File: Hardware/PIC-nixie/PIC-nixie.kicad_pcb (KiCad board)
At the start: 2 copper layers, 100 x 35 mm, 56 parts, among them J1 DX07S024WJ3R400, J2 Conn_01x20_Female, M1 TP5335, M2 TP5335, M3 TP5335, M4 TP5335, Q1 PMBTA42,185, Q2 PMBTA42,185, Q3 PMBTA42,185, Q4 PMBTA42,185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

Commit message: logic PCB tweaks, resize
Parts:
- removed the REF** at (205.0, 75.0)
- removed the REF** at (124.0, 90.0)
- added REF**: MountingHole_2.2mm_M2, MountingHole:MountingHole_2.2mm_M2, F.Cu at (125.0, 88.0)
- added REF**: MountingHole_2.2mm_M2, MountingHole:MountingHole_2.2mm_M2, F.Cu at (195.0, 88.0)
- moved SW3 37.7 mm to (136.2, 90.0)
- moved RA7 26.2 mm to (153.5, 97.4)
- moved J1 25.9 mm to (178.8, 88.5), turned to 0 degrees
- moved RA3 23.6 mm to (145.1, 97.5), turned to 270 degrees
- moved J2 22.4 mm to (161.4, 120.5)
- moved U2 21.5 mm to (121.8, 113.8)
- moved XTAL1 21.5 mm to (121.6, 109.1)
- moved C1 21.5 mm to (112.6, 96.2)
- moved C10 21.5 mm to (120.2, 104.1)
- moved C11 21.5 mm to (191.6, 118.0)
- moved C12 21.5 mm to (183.5, 99.4)
- moved C2 21.5 mm to (111.6, 117.5)
- moved C3 21.5 mm to (106.0, 106.8)
- moved C4 21.5 mm to (129.6, 106.3)
- moved C5 21.5 mm to (126.6, 108.9)
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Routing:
- net GND: track 257.5 -> 161.6 mm, vias 64 -> 65
- net Net-(RA1-Pad7): track 39.9 -> 73.4 mm
- net Net-(RA1-Pad5): track 75.8 -> 54.5 mm
- net Net-(RA1-Pad6): track 56.9 -> 68.2 mm, vias 1 -> 0
- net Net-(RA3-Pad2): track 3.22 -> 10.7 mm
- net /MIN1: track 27.8 -> 31.0 mm
- net /colon1: track 29.7 -> 26.6 mm, vias 2 -> 1
- net /HR1: track 25.9 -> 28.7 mm
- net Net-(M4-Pad1): track 11.6 -> 8.86 mm
- net Net-(M1-Pad1): track 15.6 -> 17.7 mm
- net Net-(M2-Pad1): track 13.1 -> 15.1 mm
- net VCC: track 210.8 -> 209.0 mm, vias 5 -> 6
- net Net-(M3-Pad1): track 10.6 -> 12.3 mm
- net /colon2: track 28.4 -> 30.0 mm
- net Net-(RA3-Pad3): track 15.5 -> 17.0 mm
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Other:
- board size 100 x 35 mm -> 100 x 40 mm

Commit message: PCB as submitted to fab
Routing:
- net GND: track 161.6 -> 157.7 mm
- net /MIN1: track 31.0 -> 29.9 mm
- net /HR1: track 28.7 -> 27.9 mm

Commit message: fix switch pin assignment, reduce hole size on nixie sockets
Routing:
- net Net-(RA1-Pad6): track 68.2 -> 50.9 mm, vias 0 -> 1
- net Net-(RA1-Pad5): track 54.5 -> 43.7 mm
- net Net-(RA1-Pad7): track 73.4 -> 66.1 mm, vias 1 -> 0

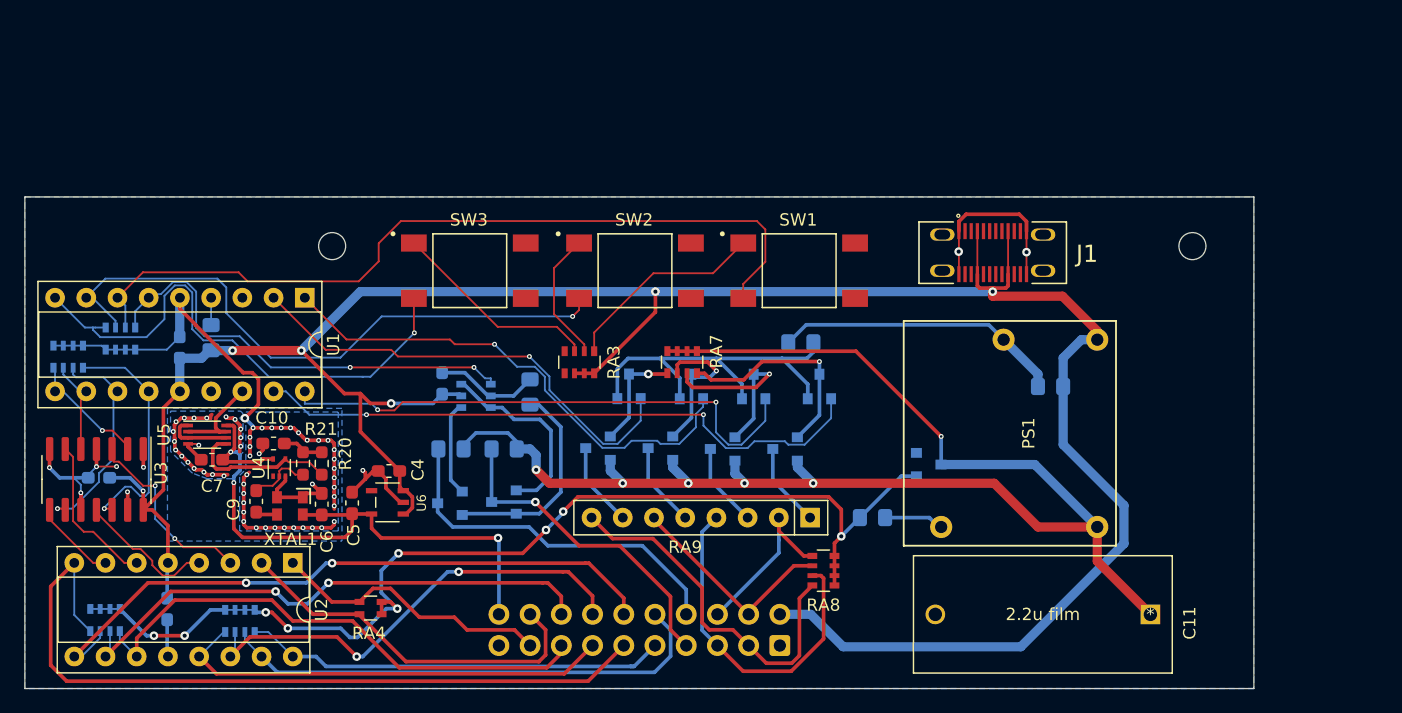
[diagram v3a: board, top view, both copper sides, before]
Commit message: add battery backup for power failures
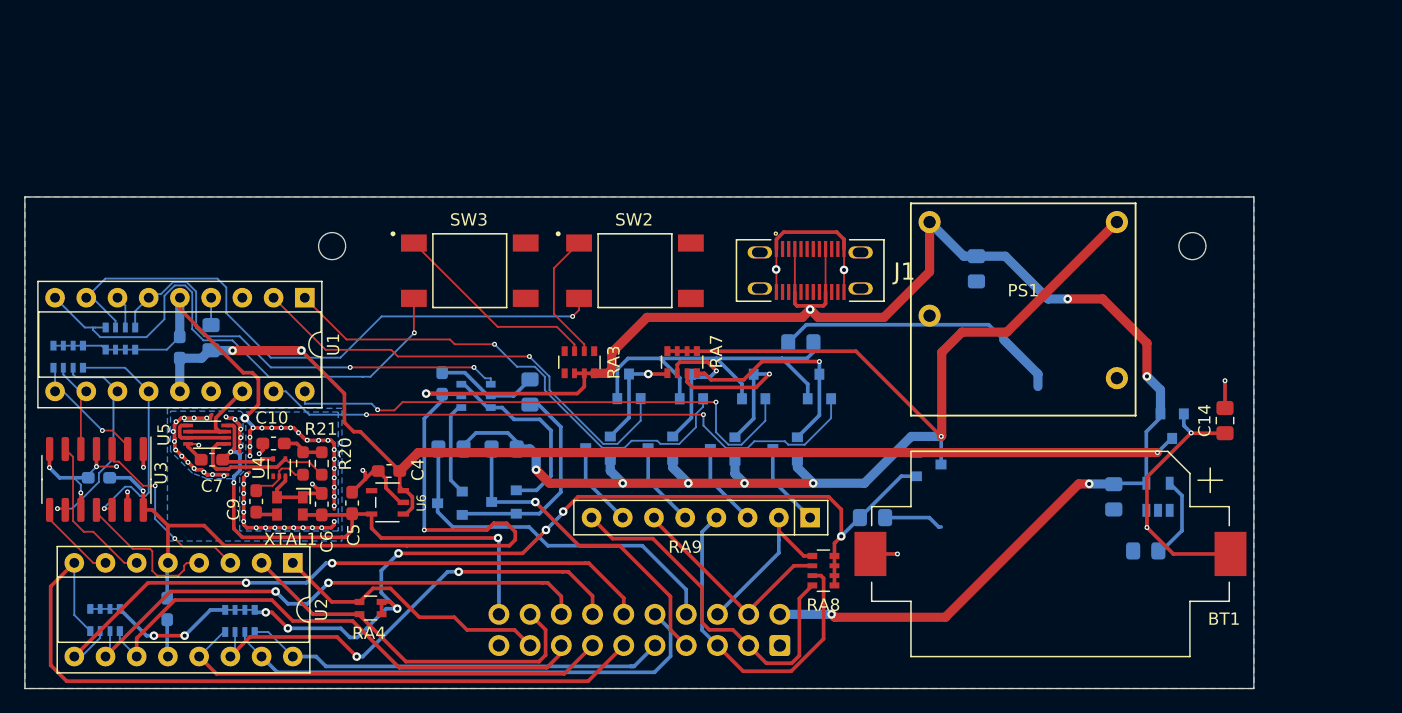
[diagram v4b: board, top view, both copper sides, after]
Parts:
- removed C11: 2.2u film, external:ECQ-E2275JB
- removed SW1: SW_SPST, external:SW_TL3301SPF260QG
- added BT1: rjd2032C1, Battery:BatteryHolder_Keystone_1060_1x2032, F.Cu at (183.4, 113.0)
- added C13: 4.7u, Capacitor_SMD:C_0805_2012Metric_Pad1.15x1.40mm_HandSolder, B.Cu at (188.6, 108.4)
- added C14: 4.7u, Capacitor_SMD:C_0805_2012Metric_Pad1.15x1.40mm_HandSolder, F.Cu at (197.7, 102.2)
- added D2: BAT54C, Package_TO_SOT_SMD:SOT-23, B.Cu at (193.3, 102.7)
- added R2: 28k, Resistor_SMD:R_0805_2012Metric_Pad1.15x1.40mm_HandSolder, B.Cu at (191.2, 112.8)
- added U8: MCP73832-2-OT, Package_TO_SOT_SMD:SOT-23-5, B.Cu at (192.2, 108.4)
- moved J1 14.9 mm to (163.9, 90.0)
- moved PS1 12.1 mm to (181.2, 91.1), turned to 0 degrees
- moved C12 11.3 mm to (177.4, 89.8), turned to 270 degrees
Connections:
- C1 pad 1: VCC -> Net-(C1-Pad1)
- C4 pad 1: VCC -> Net-(C1-Pad1)
- R1 pad 1: VCC -> Net-(C1-Pad1)
- U1 pad 14: VCC -> Net-(C1-Pad1)
- U6 pad 1: VCC -> Net-(C1-Pad1)
- U6 pad 3: VCC -> Net-(C1-Pad1)
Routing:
- net Net-(C1-Pad1): track 0.00 -> 94.8 mm, vias 0 -> 3
- net Net-(RA1-Pad7): track 66.1 -> 2.69 mm
- net Net-(BT1-Pad1): track 0.00 -> 22.9 mm, vias 0 -> 2
- net Net-(RA3-Pad1): track 16.7 -> 0.00 mm
- net Vdrive: track 117.3 -> 106.5 mm
- net VCC: track 209.0 -> 198.3 mm, vias 6 -> 8
- net Net-(R2-Pad1): track 0.00 -> 6.87 mm
- net GND: track 157.7 -> 162.1 mm, vias 65 -> 67
- net Net-(U2-Pad4): track 11.3 -> 12.3 mm

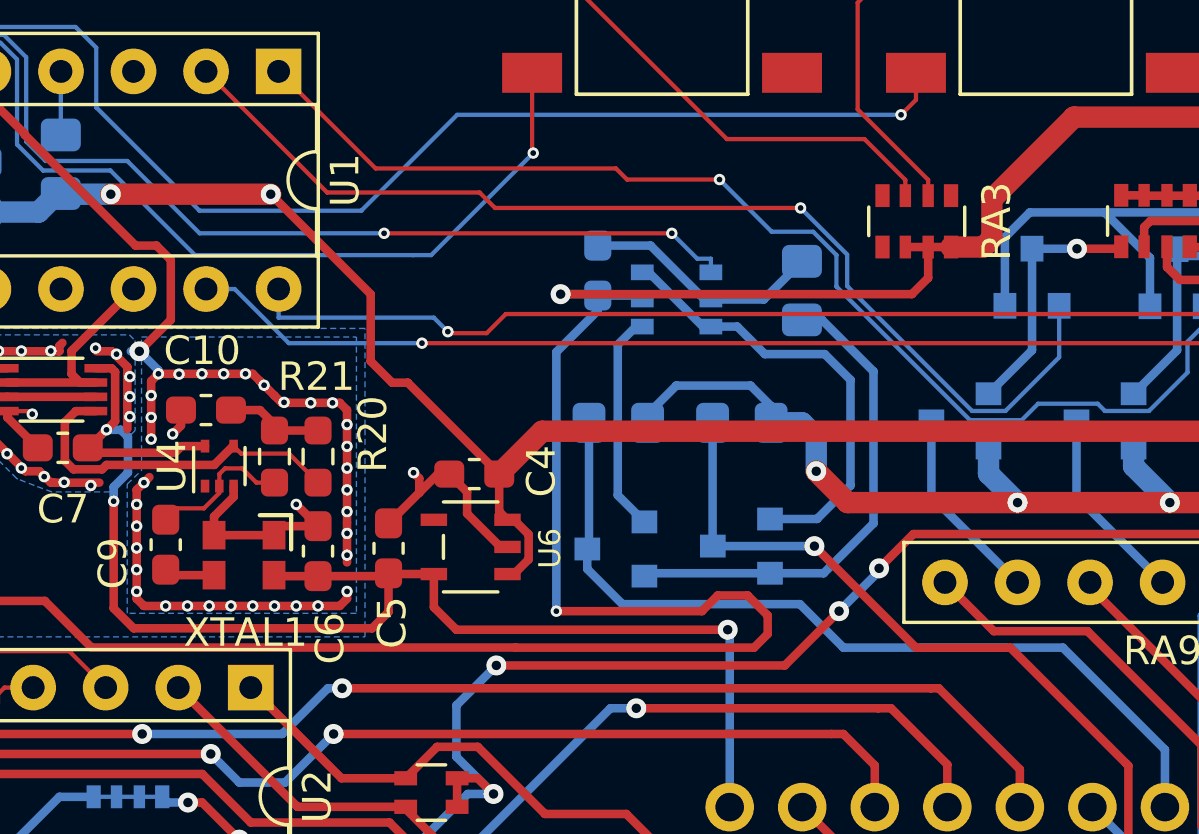
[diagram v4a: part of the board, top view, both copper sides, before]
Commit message: update 3D view, add figures
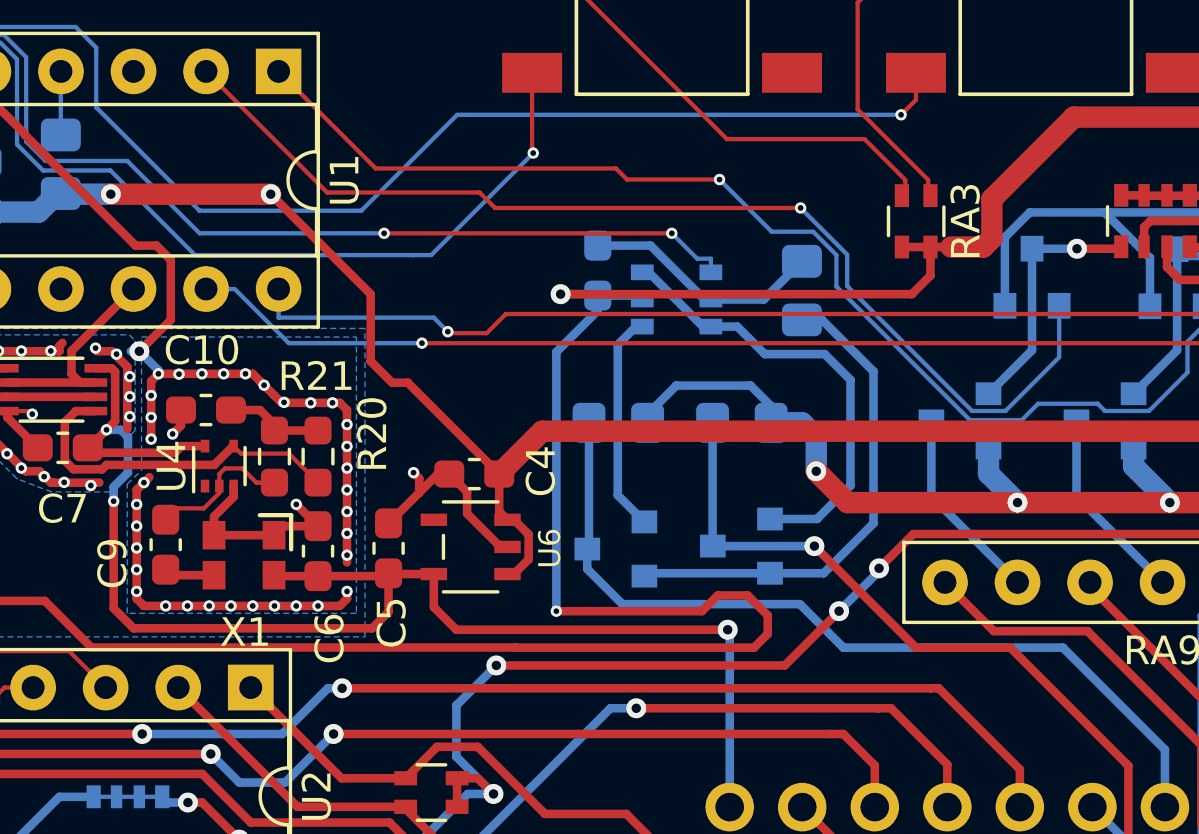
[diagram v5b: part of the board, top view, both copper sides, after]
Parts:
- RA1, RA2: value EXB-V8V103JV -> EXB-V8V104JV
- RA3: value EXB-V8V821JV -> EXB-V4V822JV; footprint Resistor_SMD:R_Array_Convex_4x0603 -> Resistor_SMD:R_Array_Convex_2x0603
- renumbered XTAL1 to X1
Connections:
- RA3 pad 3: Net-(RA3-Pad3) -> VCC
- RA3 pad 4: Net-(RA3-Pad4) -> VCC
- SW2 pad 1: Net-(RA3-Pad2) -> Net-(RA3-Pad1)
- SW3 pad 1: Net-(RA3-Pad3) -> Net-(RA3-Pad2)
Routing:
- net Net-(RA3-Pad3): track 17.0 -> 0.00 mm
- net Net-(RA3-Pad1): track 0.00 -> 10.7 mm
- net Net-(RA3-Pad2): track 10.7 -> 17.0 mm
